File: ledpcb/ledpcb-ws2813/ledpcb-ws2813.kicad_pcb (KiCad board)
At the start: 2 copper layers, 18 x 220 mm, 37 parts, among them J1 JST_XA_B04B, J2 JST_XA_B03B, J3 JST_XA_B03B

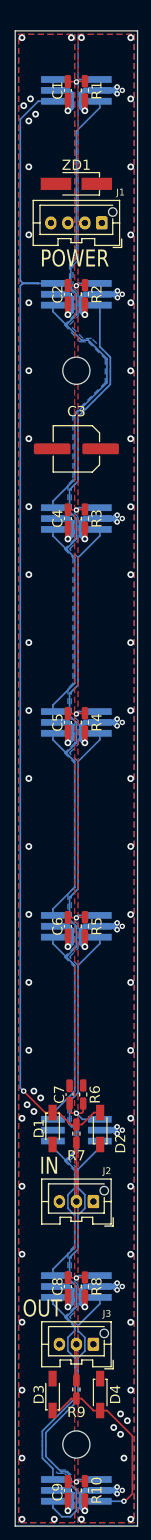
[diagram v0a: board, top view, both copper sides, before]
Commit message: Changes for ordering with JLCPCB.
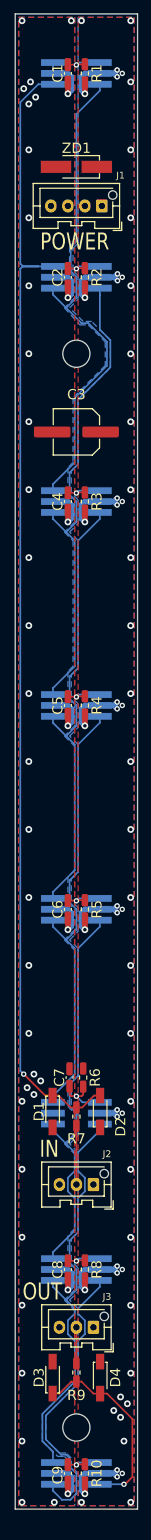
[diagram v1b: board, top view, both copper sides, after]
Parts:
- moved C1 2.50 mm to (110.8, -1.25)
- moved C2 2.50 mm to (110.8, 28.8)
- moved C3 2.50 mm to (112.0, 51.5)
- moved C4 2.50 mm to (110.8, 61.8)
- moved C5 2.50 mm to (110.8, 91.8)
- moved C6 2.50 mm to (110.8, 121.8)
- moved C7 2.50 mm to (111.0, 146.5)
- moved C8 2.50 mm to (110.8, 174.8)
- moved C9 2.50 mm to (110.8, 204.8)
- moved D1 2.50 mm to (108.5, 151.5)
- moved D2 2.50 mm to (115.5, 151.5)
- moved D3 2.50 mm to (108.5, 190.7)
- moved D4 2.50 mm to (115.5, 190.7)
- moved H1 2.50 mm to (112.0, 40.0)
- moved H2 2.50 mm to (112.0, 198.0)
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
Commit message: Merge some changes between desktop and laptop manually...
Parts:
- added REF**: JLCPCB PCBA tooling hole, ledpcb:JLCPCB PCBA tooling hole, F.Cu at (119.8, -8.75)
- added REF**: JLCPCB PCBA tooling hole, ledpcb:JLCPCB PCBA tooling hole, F.Cu at (104.2, 208.8)
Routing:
- net GND: vias 39 -> 38
- net +5V: vias 60 -> 59
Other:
- board text added: "JLCJLCJLCJLC"
- board text added: "WACCA aftermarket LED PCB replacement - using WS2813's Failure conditions: two connected LEDs broken, or final LED broken."

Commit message: replace C110526 by C2844869
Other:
- board text removed: "JLCJLCJLCJLC"
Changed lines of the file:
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@@
     (tags "Diode SMA (DO-214AC)")
     (property "JLCPCB" "")
-    (property "LCSC" "C110526")
+    (property "LCSC" "C2844869")
     (property "Package" "SMA")
     (property "Sheetfile" "ledpcb-ws2813.kicad_sch")
@@
     (effects (font (size 1.5 1.5) (thickness 0.3)))
   )
-  (gr_text "JLCJLCJLCJLC" (at 111.76 -6.35) (layer "F.SilkS")
-    (effects (font (size 1.5 1.5) (thickness 0.2)))
-  )
   (gr_text "IN" (at 108 157) (layer "F.SilkS")
     (effects (font (size 2.5 2) (thickness 0.3)))
@@
     (pts (xy 112 40) (xy 112 198))
     (height -12.25)
-    (gr_text "158.0000 mm" (at 123.1 119 90) (layer "Dwgs.User")
+    (gr_text "158,0000 mm" (at 123.1 119 90) (layer "Dwgs.User")
       (effects (font (size 1 1) (thickness 0.15)))
     )
@@
     (pts (xy 112 28.75) (xy 112 -1.25))
     (height -13)
-    (gr_text "30.0000 mm" (at 97.85 13.75 90) (layer "Dwgs.User")
+    (gr_text "30,0000 mm" (at 97.85 13.75 90) (layer "Dwgs.User")
       (effects (font (size 1 1) (thickness 0.15)))
     )
@@
     (pts (xy 112 204.75) (xy 112 174.75))
     (height -13)
-    (gr_text "30.0000 mm" (at 97.85 189.75 90) (layer "Dwgs.User")
+    (gr_text "30,0000 mm" (at 97.85 189.75 90) (layer "Dwgs.User")
       (effects (font (size 1 1) (thickness 0.15)))
     )
@@
     (pts (xy 122 15) (xy 122 40))
     (height -6.5)
-    (gr_text "25.0000 mm" (at 127.35 27.5 90) (layer "Dwgs.User")
+    (gr_text "25,0000 mm" (at 127.35 27.5 90) (layer "Dwgs.User")
       (effects (font (size 1 1) (thickness 0.15)))
     )
@@
     (pts (xy 122 -10) (xy 122 210))
     (height -10)
-    (gr_text "220.0000 mm" (at 130.85 100 90) (layer "Dwgs.User")
+    (gr_text "220,0000 mm" (at 130.85 100 90) (layer "Dwgs.User")
       (effects (font (size 1 1) (thickness 0.15)))
     )
@@
     (pts (xy 112 151.75) (xy 112 174.75))
     (height 13)
-    (gr_text "23.0000 mm" (at 97.85 163.25 90) (layer "Dwgs.User")
+    (gr_text "23,0000 mm" (at 97.85 163.25 90) (layer "Dwgs.User")
       (effects (font (size 1 1) (thickness 0.15)))
     )
@@
     (pts (xy 112 91.75) (xy 112 61.75))
     (height -13)
-    (gr_text "30.0000 mm" (at 97.85 76.75 90) (layer "Dwgs.User")
+    (gr_text "30,0000 mm" (at 97.85 76.75 90) (layer "Dwgs.User")
       (effects (font (size 1 1) (thickness 0.15)))
     )
@@
     (pts (xy 112 210) (xy 112 198))
     (height 12.25)
-    (gr_text "12.0000 mm" (at 123.1 204 90) (layer "Dwgs.User")
+    (gr_text "12,0000 mm" (at 123.1 204 90) (layer "Dwgs.User")
       (effects (font (size 1 1) (thickness 0.15)))
     )
@@
     (pts (xy 122 180) (xy 122 210))
     (height -6.5)
-    (gr_text "30.0000 mm" (at 127.35 195 90) (layer "Dwgs.User")
+    (gr_text "30,0000 mm" (at 127.35 195 90) (layer "Dwgs.User")
       (effects (font (size 1 1) (thickness 0.15)))
     )
@@
     (pts (xy 112 151.75) (xy 112 121.75))
     (height -13)
-    (gr_text "30.0000 mm" (at 97.85 136.75 90) (layer "Dwgs.User")
+    (gr_text "30,0000 mm" (at 97.85 136.75 90) (layer "Dwgs.User")
       (effects (font (size 1 1) (thickness 0.15)))
     )
@@
     (pts (xy 122 40) (xy 122 159))
     (height -6.5)
-    (gr_text "119.0000 mm" (at 127.35 99.5 90) (layer "Dwgs.User")
+    (gr_text "119,0000 mm" (at 127.35 99.5 90) (layer "Dwgs.User")
       (effects (font (size 1 1) (thickness 0.15)))
     )
@@
     (pts (xy 112 210) (xy 112 204.75))
     (height -13)
-    (gr_text "5.2500 mm" (at 97.85 207.375 90) (layer "Dwgs.User")
+    (gr_text "5,2500 mm" (at 97.85 207.375 90) (layer "Dwgs.User")
       (effects (font (size 1 1) (thickness 0.15)))
     )
@@
     (pts (xy 121 -10) (xy 103 -10))
     (height 5.099999)
-    (gr_text "18.0000 mm" (at 112 -16.249999) (layer "Dwgs.User")
+    (gr_text "18,0000 mm" (at 112 -16.249999) (layer "Dwgs.User")
       (effects (font (size 1 1) (thickness 0.15)))
     )
@@
     (pts (xy 112 -1.25) (xy 112 -10))
     (height -13)
-    (gr_text "8.7500 mm" (at 97.85 -5.625 90) (layer "Dwgs.User")
+    (gr_text "8,7500 mm" (at 97.85 -5.625 90) (layer "Dwgs.User")
       (effects (font (size 1 1) (thickness 0.15)))
     )
@@
     (pts (xy 122 159) (xy 122 180))
     (height -6.5)
-    (gr_text "21.0000 mm" (at 127.35 169.5 90) (layer "Dwgs.User")
+    (gr_text "21,0000 mm" (at 127.35 169.5 90) (layer "Dwgs.User")
       (effects (font (size 1 1) (thickness 0.15)))
     )
@@
     (pts (xy 112 121.75) (xy 112 91.75))
     (height -13)
-    (gr_text "30.0000 mm" (at 97.85 106.75 90) (layer "Dwgs.User")
+    (gr_text "30,0000 mm" (at 97.85 106.75 90) (layer "Dwgs.User")
       (effects (font (size 1 1) (thickness 0.15)))
     )
@@
     (pts (xy 122 -10) (xy 122 15))
     (height -6.5)
-    (gr_text "25.0000 mm" (at 127.35 2.5 90) (layer "Dwgs.User")
+    (gr_text "25,0000 mm" (at 127.35 2.5 90) (layer "Dwgs.User")
       (effects (font (size 1 1) (thickness 0.15)))
     )
@@
     (pts (xy 112 -10) (xy 112 40))
     (height -12.25)
-    (gr_text "50.0000 mm" (at 123.1 15 90) (layer "Dwgs.User")
+    (gr_text "50,0000 mm" (at 123.1 15 90) (layer "Dwgs.User")
       (effects (font (size 1 1) (thickness 0.15)))
     )
@@
     (pts (xy 112 61.75) (xy 112 28.75))
     (height -13)
-    (gr_text "33.0000 mm" (at 97.85 45.25 90) (layer "Dwgs.User")
-      (effects (font (size 1 1) (thickness 0.15)))
-    )
+    (gr_text "33,0000 mm" (at 97.85 45.25 90) (layer "Dwgs.User")
+      (effects (font (size 1 1) (thickness 0.15)))
+    )
